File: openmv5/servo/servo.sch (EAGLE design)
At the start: 86 parts, among them IC1 TPS613222ADBVR, IC2 AP64501SP-13, IC3 LM321LVIDCKR, IC4 74LVC1G07GW,125, J1 OPENMV5-TOP, J2 1771033, Q1 BUK6D120-60PX, U1 74LVC1G17SE-7, U2 74LVC1G17SE-7, U3 74LVC1G17SE-7, U4 74LVC1G17SE-7

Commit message: Fix servo shield part
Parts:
- C10: MPN C0402C103K5RAC -> CL05B103KB5NNNC
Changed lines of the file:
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@@
 </part>
 <part name="C10" library="0402" deviceset="CAP_0402" device="" value="10nF">
-<attribute name="MPN" value="C0402C103K5RAC"/>
+<attribute name="MPN" value="CL05B103KB5NNNC"/>
 </part>
 <part name="C12" library="0402" deviceset="CAP_0402" device="" value="2.7nF">

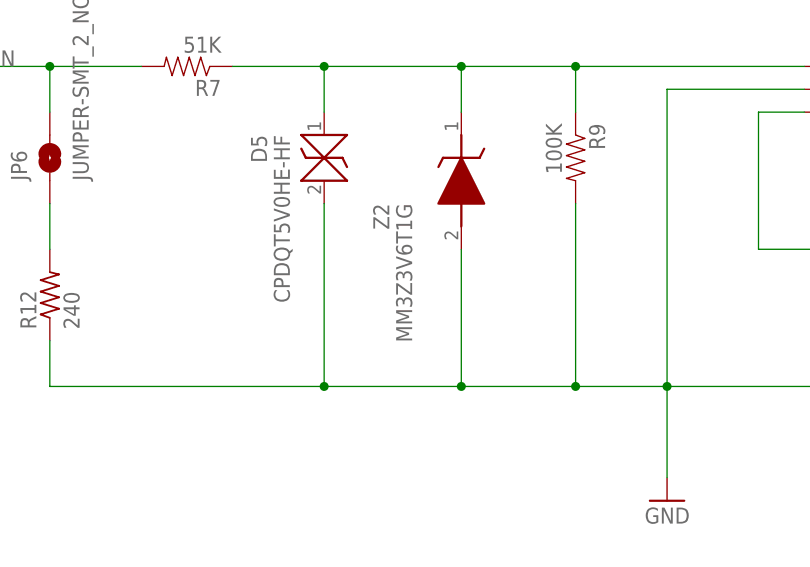
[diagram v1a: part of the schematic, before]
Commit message: Remove zener diode from ADC circuit
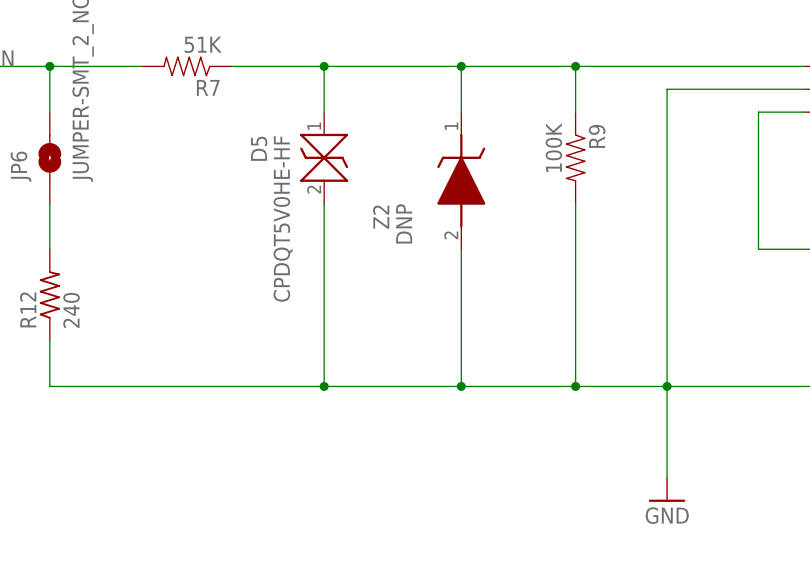
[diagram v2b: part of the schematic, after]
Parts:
- Z2: value MM3Z3V6T1G -> DNP; POPULATE (none) -> 0
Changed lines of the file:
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@@
 </part>
 <part name="GND7" library="sfe" deviceset="GND" device=""/>
-<part name="Z2" library="MM3Z3V6T1G" deviceset="MM3Z3V6T1G" device="">
+<part name="Z2" library="MM3Z3V6T1G" deviceset="MM3Z3V6T1G" device="" value="DNP">
 <attribute name="MPN" value="MM3Z3V6T1G"/>
+<attribute name="POPULATE" value="0"/>
 </part>
 <part name="R12" library="rcl" library_urn="urn:adsk.eagle:library:334" deviceset="R-US_" device="R0603" package3d_urn="urn:adsk.eagle:package:23555/3" value="240">
@@
 <attribute name="VALUE" x="308.61" y="233.68" size="1.778" layer="96" rot="MR270" align="center-left"/>
 <attribute name="MPN" x="314.96" y="243.84" size="1.778" layer="96" rot="MR270" display="off"/>
+<attribute name="POPULATE" x="314.96" y="243.84" size="1.778" layer="96" rot="MR270" display="off"/>
 </instance>
 <instance part="R12" gate="G$1" x="269.24" y="223.52" smashed="yes" rot="R90">
